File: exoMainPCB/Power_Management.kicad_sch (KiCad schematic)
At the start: 0 parts

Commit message: added power and started imu
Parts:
- added J2: Conn_02x06_Odd_Even, symbol Connector_Generic:Conn_02x06_Odd_Even
- added R8: R, symbol Device:R
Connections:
- new net +24V: J2.11 (Pin_11), J2.7 (Pin_7), J2.8 (Pin_8)
- new net +5V: J2.1 (Pin_1), J2.2 (Pin_2), R8.2
- new net GND: J2.3 (Pin_3), J2.4 (Pin_4), J2.5 (Pin_5), J2.6 (Pin_6)
- new net V_{RP}: J2.10 (Pin_10), J2.9 (Pin_9)
- new net buckStatus: J2.12 (Pin_12), R8.1
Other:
- note added: "header for 5V, 5.5A Step-Down Voltage Regulator D36V50F5 check docs at: https://www.pololu.com/product/4091"

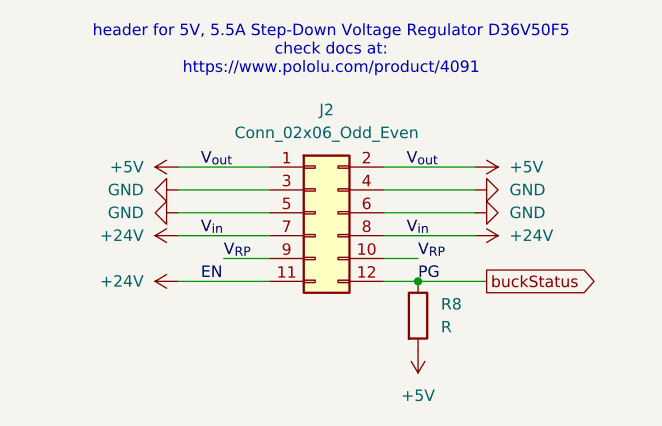
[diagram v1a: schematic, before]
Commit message: finished IMU and added component values
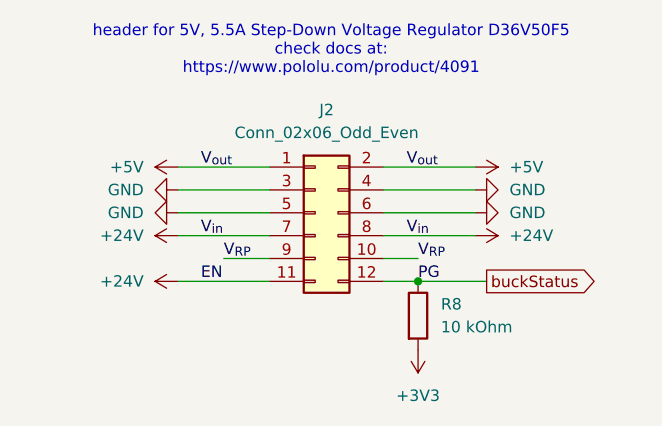
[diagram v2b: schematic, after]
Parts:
- R8: value R -> 10 kOhm
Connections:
- net +5V: no longer R8.2
- new net +3V3: R8.2
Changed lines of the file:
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@@
 			)
 		)
-		(property "Value" "R"
+		(property "Value" "10 kOhm"
 			(at 85.09 81.2799 0)
 			(effects
@@
 	)
 	(symbol
-		(lib_id "power:+5V")
+		(lib_id "power:+24V")
+		(at 88.9 71.12 270)
+		(unit 1)
+		(exclude_from_sim no)
+		(in_bom yes)
+		(on_board yes)
+		(dnp no)
+		(fields_autoplaced yes)
+		(property "Reference" "#PWR026"
+			(at 85.09 71.12 0)
+			(effects
+				(font
+					(size 1.27 1.27)
+				)
+				(hide yes)
+			)
+		)
+		(property "Value" "+24V"
+			(at 92.71 71.1199 90)
+			(effects
+				(font
+					(size 1.27 1.27)
+				)
+				(justify left)
+			)
+		)
+		(property "Footprint" ""
+			(at 88.9 71.12 0)
+			(effects
+				(font
+					(size 1.27 1.27)
+				)
+				(hide yes)
+			)
+		)
+		(property "Datasheet" ""
+			(at 88.9 71.12 0)
+			(effects
+				(font
+					(size 1.27 1.27)
+				)
+				(hide yes)
+			)
+		)
+		(property "Description" "Power symbol creates a global label with name \"+24V\""
+			(at 88.9 71.12 0)
+			(effects
+				(font
+					(size 1.27 1.27)
+				)
+				(hide yes)
+			)
+		)
+		(pin "1"
+		)
+		(instances
+			(project ""
+				(path "/d7ca945d-d48b-4d0a-95a1-7fbd3f20f475/73083210-1cbe-44f1-879c-9981ba2f953e"
+					(reference "#PWR026")
+					(unit 1)
+				)
+			)
+		)
+	)
+	(symbol
+		(lib_id "power:+24V")
+		(at 55.88 71.12 90)
+		(unit 1)
+		(exclude_from_sim no)
+		(in_bom yes)
+		(on_board yes)
+		(dnp no)
+		(fields_autoplaced yes)
+		(property "Reference" "#PWR027"
+			(at 59.69 71.12 0)
+			(effects
+				(font
+					(size 1.27 1.27)
+				)
+				(hide yes)
+			)
+		)
+		(property "Value" "+24V"
+			(at 52.07 71.1199 90)
+			(effects
+				(font
+					(size 1.27 1.27)
+				)
+				(justify left)
+			)
+		)
+		(property "Footprint" ""
+			(at 55.88 71.12 0)
+			(effects
+				(font
+					(size 1.27 1.27)
+				)
+				(hide yes)
+			)
+		)
+		(property "Datasheet" ""
+			(at 55.88 71.12 0)
+			(effects
+				(font
+					(size 1.27 1.27)
+				)
+				(hide yes)
+			)
+		)
+		(property "Description" "Power symbol creates a global label with name \"+24V\""
+			(at 55.88 71.12 0)
+			(effects
+				(font
+					(size 1.27 1.27)
+				)
+				(hide yes)
+			)
+		)
+		(pin "1"
+		)
+		(instances
+			(project "exoMainPCB"
+				(path "/d7ca945d-d48b-4d0a-95a1-7fbd3f20f475/73083210-1cbe-44f1-879c-9981ba2f953e"
+					(reference "#PWR027")
+					(unit 1)
+				)
+			)
+		)
+	)
+	(symbol
+		(lib_id "power:+24V")
+		(at 55.88 76.2 90)
+		(unit 1)
+		(exclude_from_sim no)
+		(in_bom yes)
+		(on_board yes)
+		(dnp no)
+		(fields_autoplaced yes)
+		(property "Reference" "#PWR028"
+			(at 59.69 76.2 0)
+			(effects
+				(font
+					(size 1.27 1.27)
+				)
+				(hide yes)
+			)
+		)
+		(property "Value" "+24V"
+			(at 52.07 76.1999 90)
+			(effects
+				(font
+					(size 1.27 1.27)
+				)
+				(justify left)
+			)
+		)
+		(property "Footprint" ""
+			(at 55.88 76.2 0)
+			(effects
+				(font
+					(size 1.27 1.27)
+				)
+				(hide yes)
+			)
+		)
+		(property "Datasheet" ""
+			(at 55.88 76.2 0)
+			(effects
+				(font
+					(size 1.27 1.27)
+				)
+				(hide yes)
+			)
+		)
+		(property "Description" "Power symbol creates a global label with name \"+24V\""
+			(at 55.88 76.2 0)
+			(effects
+				(font
+					(size 1.27 1.27)
+				)
+				(hide yes)
+			)
+		)
+		(pin "1"
+		)
+		(instances
+			(project "exoMainPCB"
+				(path "/d7ca945d-d48b-4d0a-95a1-7fbd3f20f475/73083210-1cbe-44f1-879c-9981ba2f953e"
+					(reference "#PWR028")
+					(unit 1)
+				)
+			)
+		)
+	)
+	(symbol
+		(lib_id "power:+3V3")
 		(at 82.55 83.82 180)
 		(unit 1)
@@
 			)
 		)
-		(property "Value" "+5V"
+		(property "Value" "+3V3"
 			(at 82.55 88.9 0)
 			(effects
@@
 			)
 		)
-		(property "Description" "Power symbol creates a global label with name \"+5V\""
+		(property "Description" "Power symbol creates a global label with name \"+3V3\""
 			(at 82.55 83.82 0)
 			(effects
@@
 		)
 		(instances
-			(project "exoMainPCB"
+			(project ""
 				(path "/d7ca945d-d48b-4d0a-95a1-7fbd3f20f475/73083210-1cbe-44f1-879c-9981ba2f953e"
 					(reference "#PWR029")
 					(unit 1)
 				)
-			)
-		)
-	)
-	(symbol
-		(lib_id "power:+24V")
-		(at 88.9 71.12 270)
-		(unit 1)
-		(exclude_from_sim no)
-		(in_bom yes)
-		(on_board yes)
-		(dnp no)
-		(fields_autoplaced yes)
-		(property "Reference" "#PWR026"
-			(at 85.09 71.12 0)
-			(effects
-				(font
-					(size 1.27 1.27)
-				)
-				(hide yes)
-			)
-		)
-		(property "Value" "+24V"
-			(at 92.71 71.1199 90)
-			(effects
-				(font
-					(size 1.27 1.27)
-				)
-				(justify left)
-			)
-		)
-		(property "Footprint" ""
-			(at 88.9 71.12 0)
-			(effects
-				(font
-					(size 1.27 1.27)
-				)
-				(hide yes)
-			)
-		)
-		(property "Datasheet" ""
-			(at 88.9 71.12 0)
-			(effects
-				(font
-					(size 1.27 1.27)
-				)
-				(hide yes)
-			)
-		)
-		(property "Description" "Power symbol creates a global label with name \"+24V\""
-			(at 88.9 71.12 0)
-			(effects
-				(font
-					(size 1.27 1.27)
-				)
-				(hide yes)
-			)
-		)
-		(pin "1"
-		)
-		(instances
-			(project ""
-				(path "/d7ca945d-d48b-4d0a-95a1-7fbd3f20f475/73083210-1cbe-44f1-879c-9981ba2f953e"
-					(reference "#PWR026")
-					(unit 1)
-				)
-			)
-		)
-	)
-	(symbol
-		(lib_id "power:+24V")
-		(at 55.88 71.12 90)
-		(unit 1)
-		(exclude_from_sim no)
-		(in_bom yes)
-		(on_board yes)
-		(dnp no)
-		(fields_autoplaced yes)
-		(property "Reference" "#PWR027"
-			(at 59.69 71.12 0)
-			(effects
-				(font
-					(size 1.27 1.27)
-				)
-				(hide yes)
-			)
-		)
-		(property "Value" "+24V"
-			(at 52.07 71.1199 90)
-			(effects
-				(font
-					(size 1.27 1.27)
-				)
-				(justify left)
-			)
-		)
-		(property "Footprint" ""
-			(at 55.88 71.12 0)
-			(effects
-				(font
-					(size 1.27 1.27)
-				)
-				(hide yes)
-			)
-		)
-		(property "Datasheet" ""
-			(at 55.88 71.12 0)
-			(effects
-				(font
-					(size 1.27 1.27)
-				)
-				(hide yes)
-			)
-		)
-		(property "Description" "Power symbol creates a global label with name \"+24V\""
-			(at 55.88 71.12 0)
-			(effects
-				(font
-					(size 1.27 1.27)
-				)
-				(hide yes)
-			)
-		)
-		(pin "1"
-		)
-		(instances
-			(project "exoMainPCB"
-				(path "/d7ca945d-d48b-4d0a-95a1-7fbd3f20f475/73083210-1cbe-44f1-879c-9981ba2f953e"
-					(reference "#PWR027")
-					(unit 1)
-				)
-			)
-		)
-	)
-	(symbol
-		(lib_id "power:+24V")
-		(at 55.88 76.2 90)
-		(unit 1)
-		(exclude_from_sim no)
-		(in_bom yes)
-		(on_board yes)
-		(dnp no)
-		(fields_autoplaced yes)
-		(property "Reference" "#PWR028"
-			(at 59.69 76.2 0)
-			(effects
-				(font
-					(size 1.27 1.27)
-				)
-				(hide yes)
-			)
-		)
-		(property "Value" "+24V"
-			(at 52.07 76.1999 90)
-			(effects
-				(font
-					(size 1.27 1.27)
-				)
-				(justify left)
-			)
-		)
-		(property "Footprint" ""
-			(at 55.88 76.2 0)
-			(effects
-				(font
-					(size 1.27 1.27)
-				)
-				(hide yes)
-			)
-		)
-		(property "Datasheet" ""
-			(at 55.88 76.2 0)
-			(effects
-				(font
-					(size 1.27 1.27)
-				)
-				(hide yes)
-			)
-		)
-		(property "Description" "Power symbol creates a global label with name \"+24V\""
-			(at 55.88 76.2 0)
-			(effects
-				(font
-					(size 1.27 1.27)
-				)
-				(hide yes)
-			)
-		)
-		(pin "1"
-		)
-		(instances
-			(project "exoMainPCB"
-				(path "/d7ca945d-d48b-4d0a-95a1-7fbd3f20f475/73083210-1cbe-44f1-879c-9981ba2f953e"
-					(reference "#PWR028")
-					(unit 1)
-				)

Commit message: changed all resistors to US, updated IO, finished Handheld
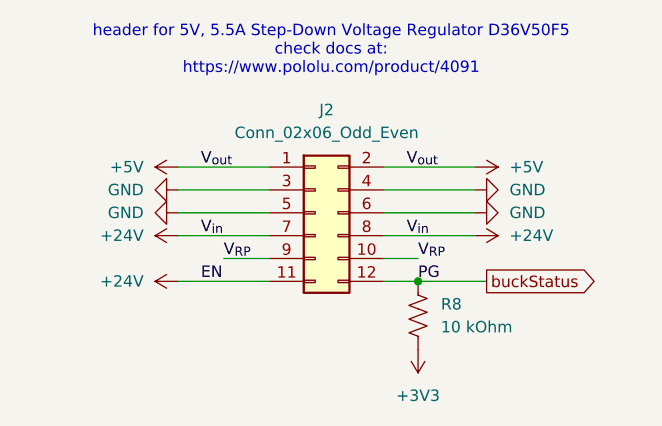
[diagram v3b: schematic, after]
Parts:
- R8: symbol Device:R -> Device:R_US
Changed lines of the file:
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@@
 	)
 	(symbol
-		(lib_id "Device:R")
+		(lib_id "Device:R_US")
 		(at 82.55 80.01 0)
 		(unit 1)
